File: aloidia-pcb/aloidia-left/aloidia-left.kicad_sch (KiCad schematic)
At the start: 225 parts, among them J1 SWD_02x05_1.27mm, J10 Pin headers 2.54mm 01x02, J11 USB4105-GF-A-120, J12 SM08B-SRSS-TB(LF)(SN), J2 SM08B-SRSS-TB(LF)(SN), J3 SM06B-SRSS-TB, J4 SM03B-SRSS-TB(LF)(SN), J5 Picoblade 0532614002, J6 Pin headers 2.54mm 01x03, J7 USB4105-GF-A-120, J9 SM04B-SRSS-TB(LF)(SN), Q1 PJA3404, Q2 DMG9926UDM, Q3 Si2371EDS, Q4 Si2371EDS, Q5 PJA3404, SW1 SSSS213100, SW100 MX_EC11, SW101 SW_Push, SW102 SW_Push, SW103 SW_Push, SW104 SW_Push, SW105 SW_Push, SW106 SW_Push, SW107 SW_Push, SW108 SW_Push, SW110 SW_Push, SW111 SW_Push, SW112 SW_Push, SW113 SW_Push, SW114 SW_Push, SW115 SW_Push, SW116 SW_Push, SW117 SW_Push, SW120 SW_Push, SW121 SW_Push, SW122 SW_Push, SW123 SW_Push, SW124 SW_Push, SW125 SW_Push, SW126 SW_Push, SW127 SW_Push, SW130 SW_Push, SW131 SW_Push, SW132 SW_Push, SW133 SW_Push, SW134 SW_Push, SW135 SW_Push, SW136 SW_Push, SW137 SW_Push, SW140 SW_Push, SW141 SW_Push, SW142 SW_Push, SW143 SW_Push, SW144 SW_Push, SW145 SW_Push, SW146 SW_Push, SW147 MX_EVQWGD001, SW2 EG6201, SW243 SW_Push, SW244 SW_Push, SW246 SW_Push, U1 MAX17048, U2 MDBT50Q-1MV2, U3 MCP1812AT-033/TT, U4 DMN2004DMK-7, U5 BQ24075RGT, U6 AP9101CK6-ANTRG1, U7 STS234050UL30, U8 BQ25504, U9 LTC4359-MS8, Y1 32.768kHz

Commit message: Replaced usb by THT and reverse mounted
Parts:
- H1, H2, H3, H4, H5, H6: value 3.2mm_M3 -> 2.2mm_M2; footprint MountingHole:MountingHole_3.2mm_M3_Pad -> MountingHole:MountingHole_2.2mm_M2_Pad
- J11, J7: value USB4105-GF-A-120 -> USB4085-GF-A; footprint Connector_USB:USB_C_Receptacle_HRO_TYPE-C-31-M-12 -> Connector_USB:USB_C_Receptacle_GCT_USB4085; Digikey ref (none) -> 2073-USB4085-GF-ACT-ND; Manufacturer ref USB4105-GF-A-120 -> USB4085-GF-A; Mouser ref 640-USB4105-GF-A-120 -> (none)
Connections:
- net +3.3V: now also J12.7 (Pin_7), J2.7 (Pin_7); no longer J12.2 (Pin_2), J2.2 (Pin_2)
- net +BATT_PULLUP: now also SW1.3 (C); no longer SW1.1 (A)
- net BUSY: now also J12.1 (Pin_1), J2.1 (Pin_1), U2.41 (P0.17); no longer J12.8 (Pin_8), J2.8 (Pin_8), U2.46 (P0.22)
- net CS: now also J12.4 (Pin_4), J2.4 (Pin_4), U2.44 (P0.20); no longer J12.5 (Pin_5), J2.5 (Pin_5), U2.43 (P0.21)
- net DC: now also J12.3 (Pin_3), J2.3 (Pin_3), U2.43 (P0.21); no longer J12.6 (Pin_6), J2.6 (Pin_6), U2.44 (P0.20)
- net DIN: now also J12.6 (Pin_6), J2.6 (Pin_6), U2.46 (P0.22); no longer J12.3 (Pin_3), J2.3 (Pin_3), U2.41 (P0.17)
- net GND: now also J12.8 (Pin_8), J2.8 (Pin_8), SW1.1 (A); no longer J12.1 (Pin_1), J2.1 (Pin_1), SW1.3 (C)
- net RST: now also J12.2 (Pin_2), J2.2 (Pin_2), U2.42 (P0.19); no longer J12.7 (Pin_7), J2.7 (Pin_7), U2.45 (P0.23)
- net SCK: now also J12.5 (Pin_5), J2.5 (Pin_5), U2.45 (P0.23); no longer J12.4 (Pin_4), J2.4 (Pin_4), U2.42 (P0.19)

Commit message: Added graphic elements
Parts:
- added G1: Aloidia_Logo, 0_various:aloidia_logo, symbol 0_various:Aloidia_Logo
- JP1: value REV_PROT_DISABLE -> OVCH_PROT_DISABLE
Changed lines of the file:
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@@
     (in_bom no) (on_board yes) (fields_autoplaced)
     (property "Reference" "JP1" (id 0) (at 302.26 275.59 0))
-    (property "Value" "REV_PROT_DISABLE" (id 1) (at 302.26 278.13 0))
+    (property "Value" "OVCH_PROT_DISABLE" (id 1) (at 302.26 278.13 0))
     (property "Footprint" "Jumper:SolderJumper-2_P1.3mm_Open_TrianglePad1.0x1.5mm" (id 2) (at 302.26 281.94 0)
       (effects (font (size 1.27 1.27)) hide)
@@
     (pin "2")
   )
+  (symbol (lib_id "0_various:Aloidia_Logo") (at 413.385 126.365 0) (unit 1)
+    (in_bom yes) (on_board yes) (fields_autoplaced)
+    (property "Reference" "G1" (id 0) (at 459.74 129.0535 0)
+      (effects (font (size 1.27 1.27)) (justify left))
+    )
+    (property "Value" "Aloidia_Logo" (id 1) (at 459.74 131.5935 0)
+      (effects (font (size 1.27 1.27)) (justify left))
+    )
+    (property "Footprint" "0_various:aloidia_logo" (id 2) (at 413.385 126.365 0)
+      (effects (font (size 1.27 1.27)) hide)
+    )
+    (property "Datasheet" "" (id 3) (at 413.385 126.365 0)
+      (effects (font (size 1.27 1.27)) hide)
+    )
+  )
   (symbol (lib_id "Device:R") (at 493.395 210.185 90) (unit 1)
     (in_bom yes) (on_board yes)
@@
       (reference "FB2") (unit 1) (value "MH2029-600Y") (footprint "Inductor_SMD:L_0805_2012Metric")
     )
+    (path "/943537da-bd41-4632-9fff-07c64a6cff6c"
+      (reference "G1") (unit 1) (value "Aloidia_Logo") (footprint "0_various:aloidia_logo")
+    )
     (path "/584e654a-fe43-413a-84de-c3889938e191"
       (reference "H1") (unit 1) (value "2.2mm_M2") (footprint "MountingHole:MountingHole_2.2mm_M2_Pad")
@@
     )
     (path "/6cdd3c99-5837-4b31-8029-55819d65dd32"
-      (reference "JP1") (unit 1) (value "REV_PROT_DISABLE") (footprint "Jumper:SolderJumper-2_P1.3mm_Open_TrianglePad1.0x1.5mm")
+      (reference "JP1") (unit 1) (value "OVCH_PROT_DISABLE") (footprint "Jumper:SolderJumper-2_P1.3mm_Open_TrianglePad1.0x1.5mm")
     )
     (path "/908ca2a8-06e2-4247-b412-abb08a4f25fd"

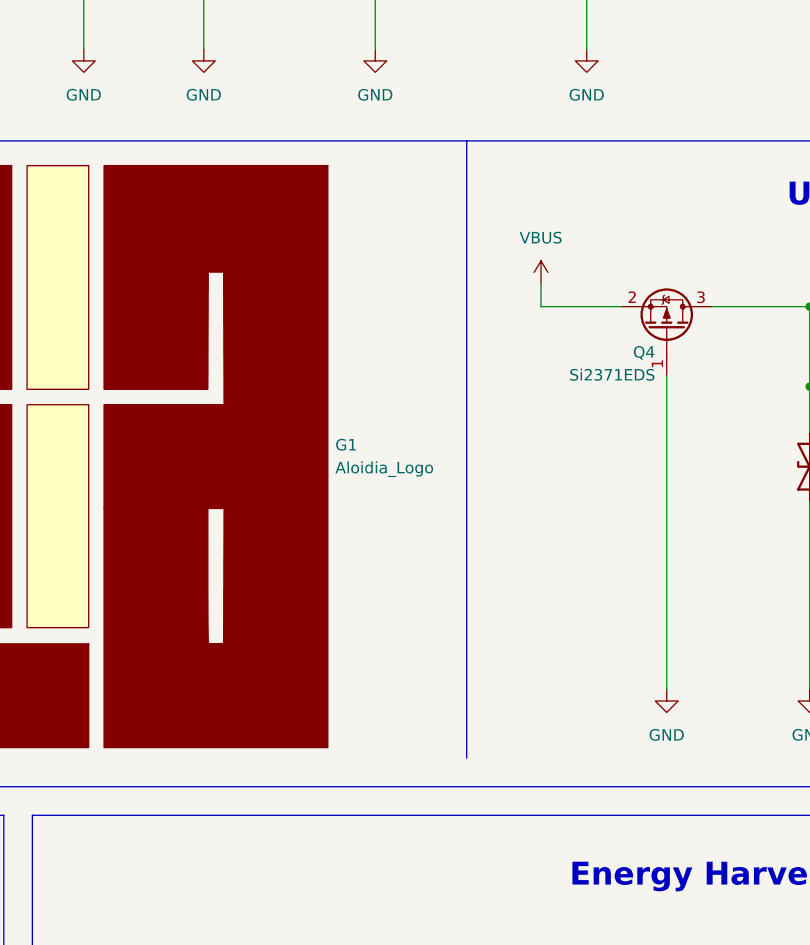
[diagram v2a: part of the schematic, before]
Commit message: Added left/right text on schematic
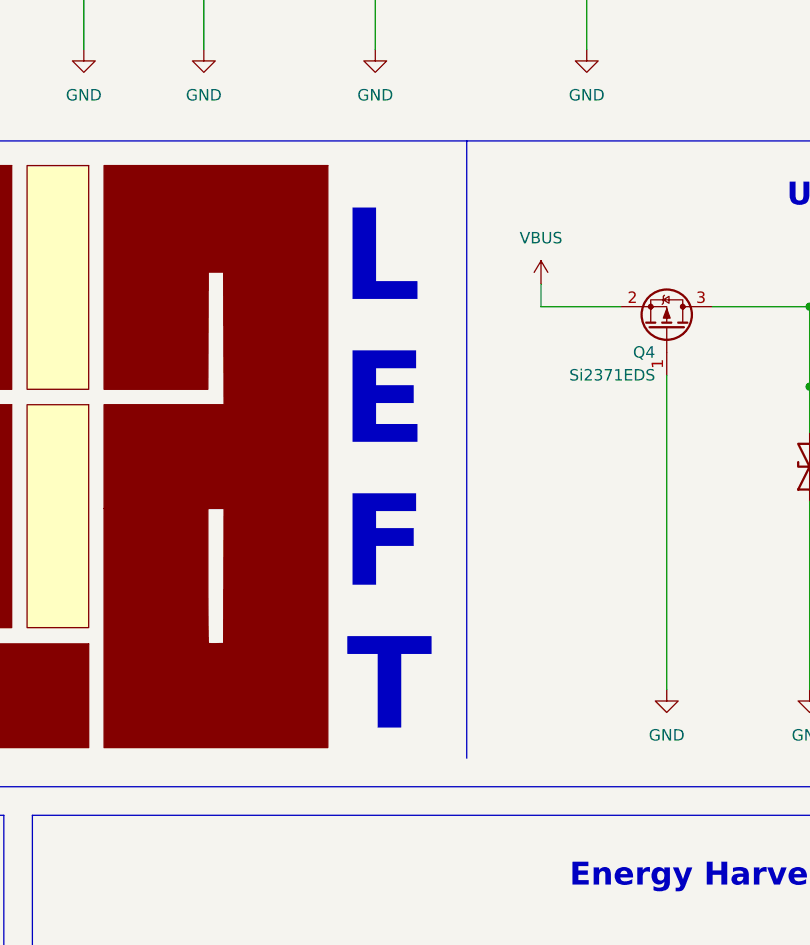
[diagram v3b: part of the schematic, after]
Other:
- note added: "E"
- note added: "F"
- note added: "L"
- note added: "T"
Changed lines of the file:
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@@
     (effects (font (size 2.54 2.54) (thickness 0.508) bold) (justify left bottom))
   )
+  (text "F" (at 460.375 146.05 0)
+    (effects (font (size 10.16 10.16) (thickness 2.54) bold) (justify left bottom))
+  )
   (text "MX Switch + Horizontal Encoder" (at 163.83 193.675 0)
     (effects (font (size 2.54 2.54) (thickness 0.508) bold) (justify left bottom))
@@
     (effects (font (size 1.27 1.27)) (justify left bottom))
   )
+  (text "E" (at 460.375 130.175 0)
+    (effects (font (size 10.16 10.16) (thickness 2.54) bold) (justify left bottom))
+  )
   (text "Energy Harvester" (at 485.775 178.435 0)
     (effects (font (size 2.54 2.54) (thickness 0.508) bold) (justify left bottom))
   )
+  (text "T" (at 461.01 161.925 0)
+    (effects (font (size 10.16 10.16) (thickness 2.54) bold) (justify left bottom))
+  )
   (text "MX Switch + EC11 Encoder" (at 168.275 146.05 0)
     (effects (font (size 2.54 2.54) (thickness 0.508) bold) (justify left bottom))
@@
     (effects (font (size 1.27 1.27)) (justify left bottom))
   )
+  (text "L" (at 460.375 114.3 0)
+    (effects (font (size 10.16 10.16) (thickness 2.54) bold) (justify left bottom))
+  )
   (text "Navigation switch/Encoder selection" (at 264.795 146.05 0)
     (effects (font (size 2.54 2.54) (thickness 0.508) bold) (justify left bottom))
@@
     (in_bom yes) (on_board yes) (fields_autoplaced)
     (property "Reference" "G1" (id 0) (at 459.74 129.0535 0)
-      (effects (font (size 1.27 1.27)) (justify left))
+      (effects (font (size 1.27 1.27)) (justify left) hide)
     )
-    (property "Value" "Aloidia_Logo" (id 1) (at 459.74 131.5935 0)
-      (effects (font (size 1.27 1.27)) (justify left))
+    (property "Value" "Aloidia_Logo" (id 1) (at 459.74 130.3235 0)
+      (effects (font (size 1.27 1.27)) (justify left) hide)
     )
     (property "Footprint" "0_various:aloidia_logo" (id 2) (at 413.385 126.365 0)
